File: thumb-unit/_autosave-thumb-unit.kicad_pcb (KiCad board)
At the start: 2 copper layers, 82.5 x 79 mm, 24 parts, among them J1 Conn_01x10, SW1 SW_SPDT, SW2 SW_Push, SW3 SW_Push, SW4 SW_Push, SW5 SW_Push, U1 xiao-ble, U2 PMW3610, U3 TLV70218_SOT23-5

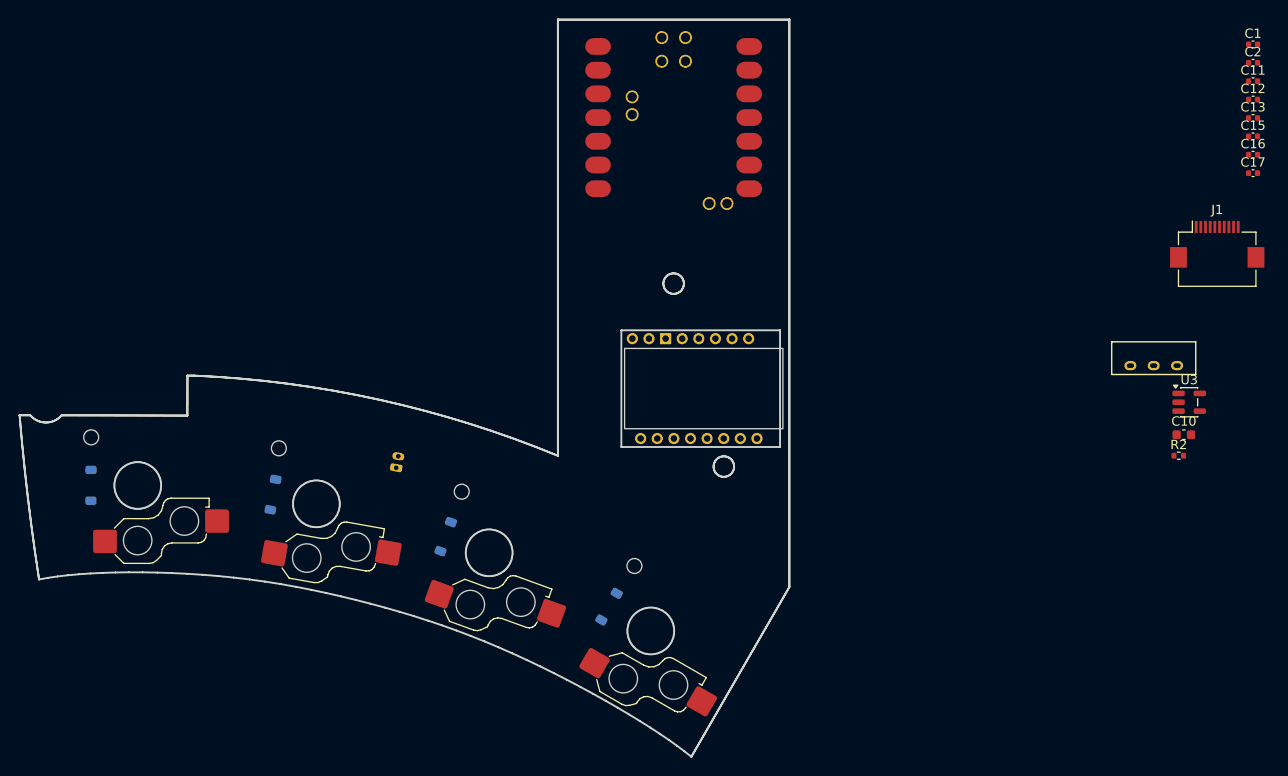
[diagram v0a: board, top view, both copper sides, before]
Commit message: fix: 親指ユニットの回路図
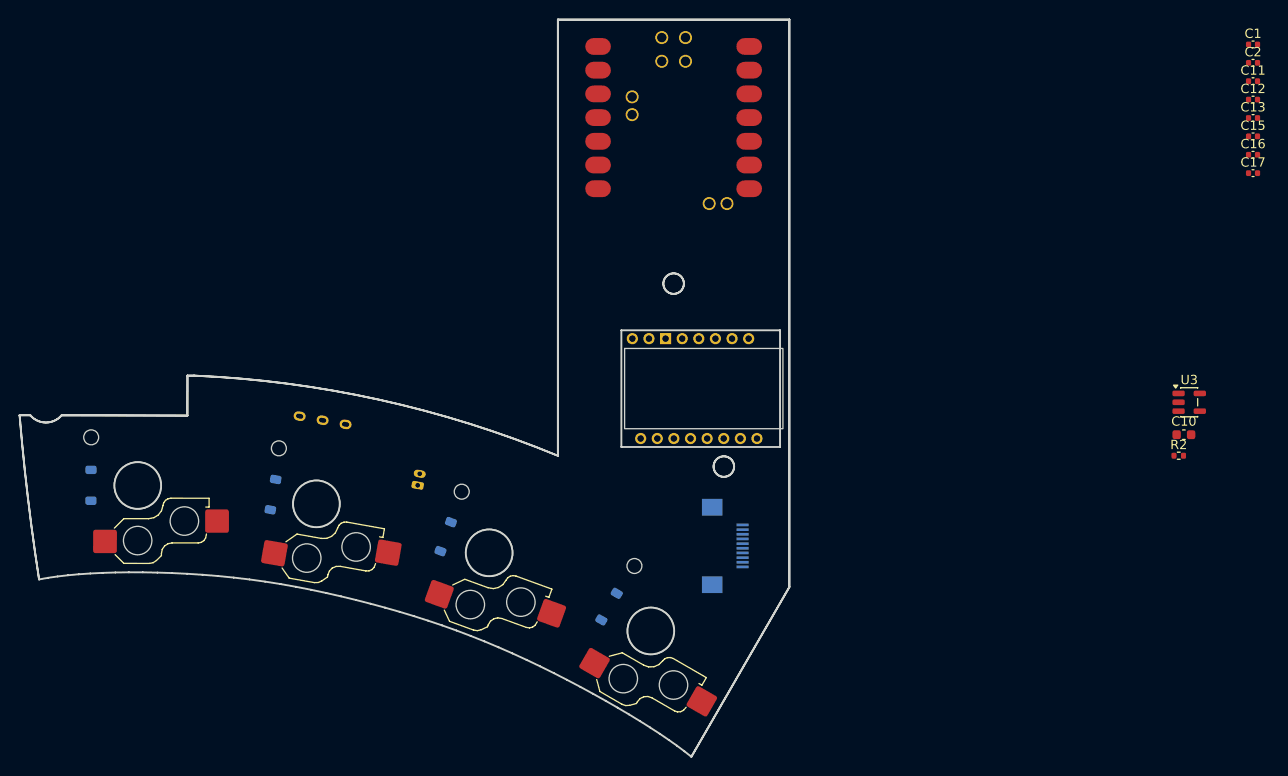
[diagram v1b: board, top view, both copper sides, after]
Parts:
- J1, SW1: moved to B.Cu
- moved SW1 89.0 mm to (105.0, 141.5), turned to 169.9 degrees
- moved J1 61.8 mm to (147.9, 156.0), turned to 90 degrees
- moved BT1 2.97 mm to (115.0, 149.5)
